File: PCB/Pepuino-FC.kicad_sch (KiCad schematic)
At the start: 85 parts, among them CN1 XT30UPB-M, M1 Motor_Servo, M2 Motor_Servo, M3 Motor_Servo, M4 Motor_Servo, M5 Motor_Servo, M6 Motor_Servo, SW1 TS-1088-AR02016, SW2 TS-1088-AR02016, U1 STM32F722RETx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

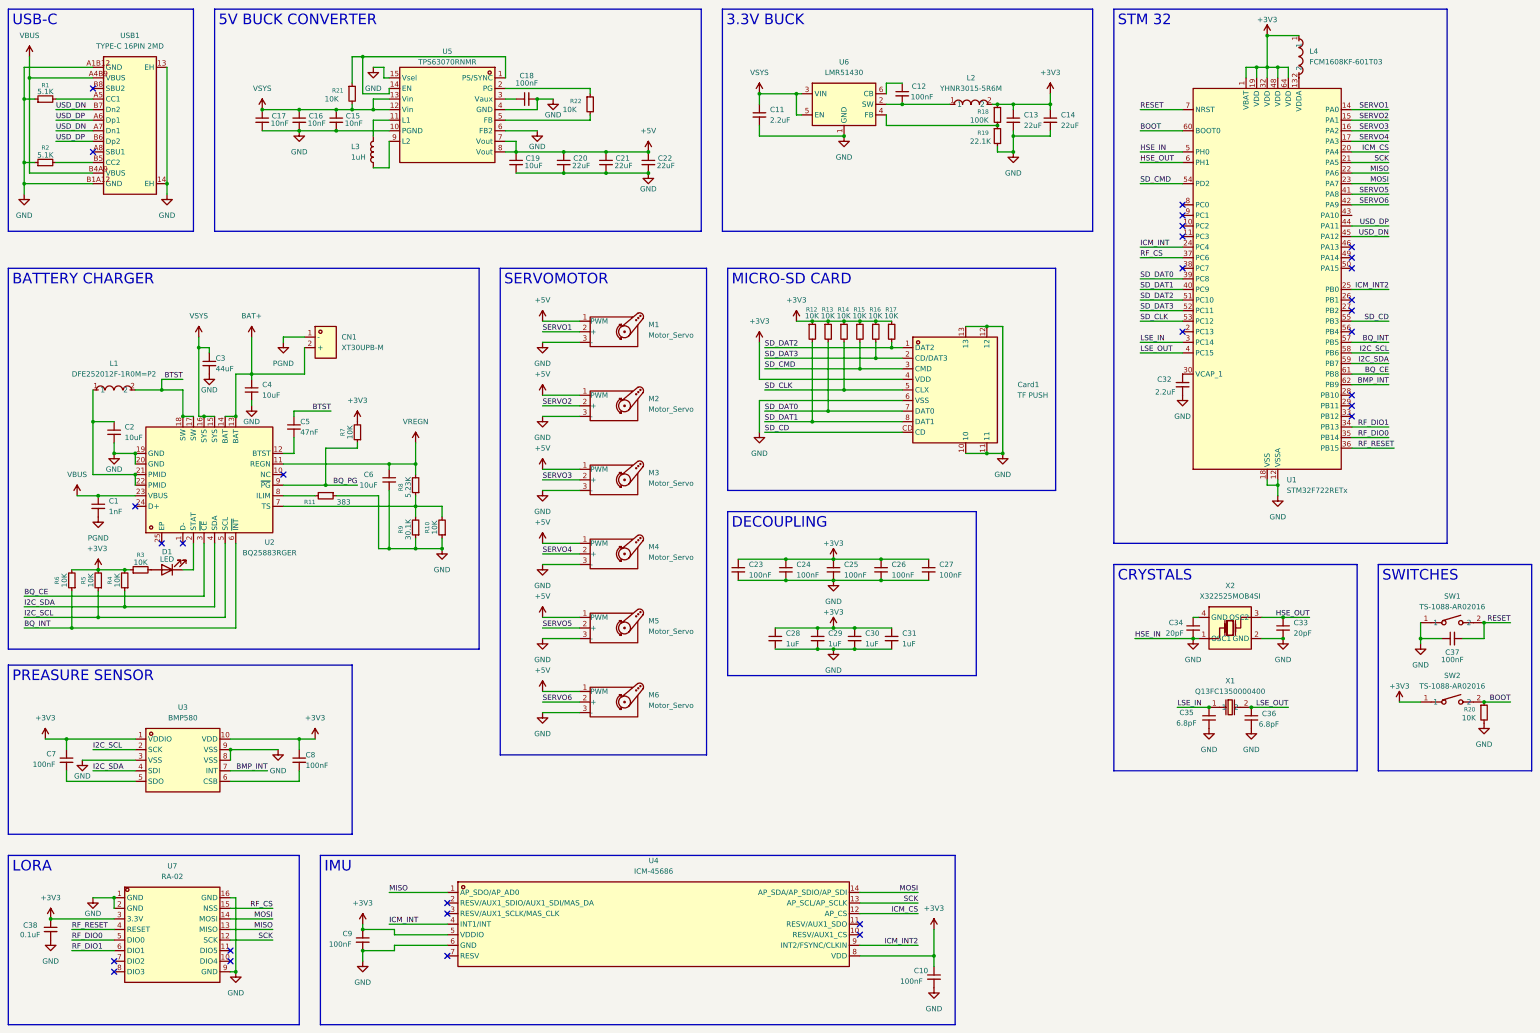
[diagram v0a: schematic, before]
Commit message: add pyro
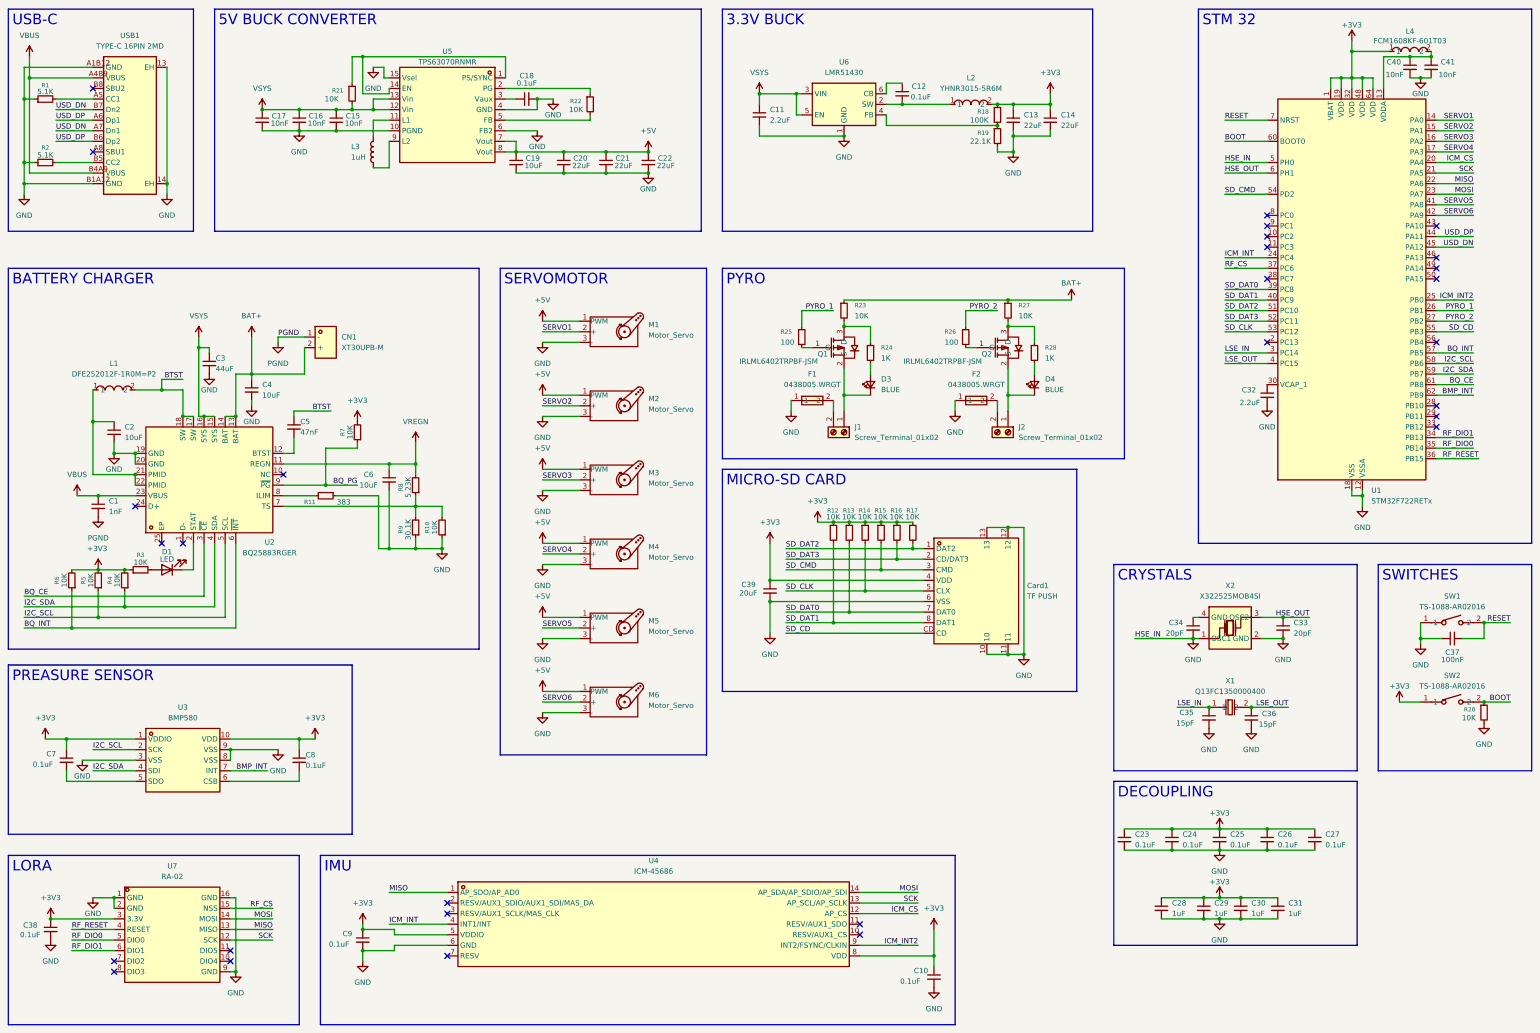
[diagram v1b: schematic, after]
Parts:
- added C39: 20uF, Capacitor_SMD:C_0402_1005Metric, symbol Device:C_Small
- added C40, C41: 10nF, Capacitor_SMD:C_0402_1005Metric, symbol Device:C_Small
- added D3, D4: BLUE, symbol Device:LED_Small
- added F1, F2: 0438005.WRGT, easyEDA:F0603, symbol easyeda2kicad:0438005.WRGT
- added J1, J2: Screw_Terminal_01x02, symbol Connector:Screw_Terminal_01x02
- added Q1, Q2: IRLML6402TRPBF-JSM, easyEDA:SOT-23-3_L2.9-W1.3-P1.90-LS2.4-BR, symbol easyeda2kicad:IRLML6402TRPBF-JSM
- added R23, R27: 10K, Resistor_SMD:R_0201_0603Metric, symbol Device:R_Small
- added R24, R28: 1K, Resistor_SMD:R_0201_0603Metric, symbol Device:R_Small
- added R25, R26: 100, Resistor_SMD:R_0201_0603Metric, symbol Device:R_Small
- C10, C12, C18, C23, C24, C25, C26, C27, C7, C8, C9: value 100nF -> 0.1uF
- C35, C36: value 6.8pF -> 15pF
- CN1: footprint easyeda2kicad:CONN-TH_XT30UPB-M -> easyEDA:CONN-TH_XT30UPB-M
- Card1: footprint easyeda2kicad:TF-SMD_TF-PUSH -> easyEDA:TF-SMD_TF-PUSH
- D1: footprint (none) -> LED_SMD:LED_0603_1608Metric
- L1: footprint easyeda2kicad:L2520 -> easyEDA:L2520
- L2: footprint easyeda2kicad:IND-SMD_L3.0-W3.0 -> easyEDA:IND-SMD_L3.0-W3.0
- L3: footprint (none) -> Inductor_SMD:L_0402_1005Metric
- L4: footprint easyeda2kicad:L0603 -> easyEDA:L0603
- SW1, SW2: footprint easyeda2kicad:SW-SMD_L3.9-W3.0-P4.45 -> easyEDA:SW-SMD_L3.9-W3.0-P4.45
- U2: footprint easyeda2kicad:VFQFPN-24_L4.0-W4.0-P0.50-BL-EP2.8 -> easyEDA:VFQFPN-24_L4.0-W4.0-P0.50-BL-EP2.8
- U3: footprint easyeda2kicad:LGA-10_L2.0-W2.0-P0.50-TL_BMP580 -> easyEDA:LGA-10_L2.0-W2.0-P0.50-TL_BMP580
- U4: footprint easyeda2kicad:LGA-14_L3.0-W2.5-P0.50-TL -> easyEDA:LGA-14_L3.0-W2.5-P0.50-TL
- U5: footprint easyeda2kicad:VQFN-15_L3.0-W2.5-P0.50-BL -> (none)
- U7: footprint easyeda2kicad:WIRELM-SMD_RA-02-BL -> easyEDA:WIRELM-SMD_RA-02-BL
- USB1: footprint easyeda2kicad:USB-C-SMD_TYPE-C-16PIN-2MD-073 -> easyEDA:USB-C-SMD_TYPE-C-16PIN-2MD-073
- X1: footprint easyeda2kicad:FC-135R_L3.2-W1.5 -> easyEDA:FC-135R_L3.2-W1.5
- X2: footprint easyeda2kicad:CRYSTAL-SMD_4P-L3.2-W2.5-BL -> easyEDA:CRYSTAL-SMD_4P-L3.2-W2.5-BL
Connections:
- net +3V3: now also C39.1
- net BAT+: now also R23.1, R27.1
- net GND: now also C39.2, C40.2, C41.2, F1.1, F2.1
- net at L4.2, U1.13 (VDDA): now also C40.1, C41.1
- net PYRO_1: now reaches U1.26 (PB1)
- net PYRO_1: now also R25.1
- net PYRO_2: now reaches U1.27 (PB2)
- net PYRO_2: now also R26.1
- new net: D3.1 (K), J1.1 (Pin_1), Q1.2 (S)
- new net: D3.2 (A), R24.2
- new net: Q1.1 (G), R25.2
- new net: F2.2, J2.2 (Pin_2)
- new net: Q2.1 (G), R26.2
- new net: D4.1 (K), J2.1 (Pin_1), Q2.2 (S)
- new net: Q2.3 (D), R27.2, R28.1
- new net: Q1.3 (D), R23.2, R24.1
- new net: F1.2, J1.2 (Pin_2)
- new net: D4.2 (A), R28.2
- no-connect marks 30 -> 29
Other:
- moved on the sheet: C23, C24, C25, C26, C27, C28, C29, C30, C31, C32, Card1, L4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
